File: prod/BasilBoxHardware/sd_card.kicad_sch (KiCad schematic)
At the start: 1 part

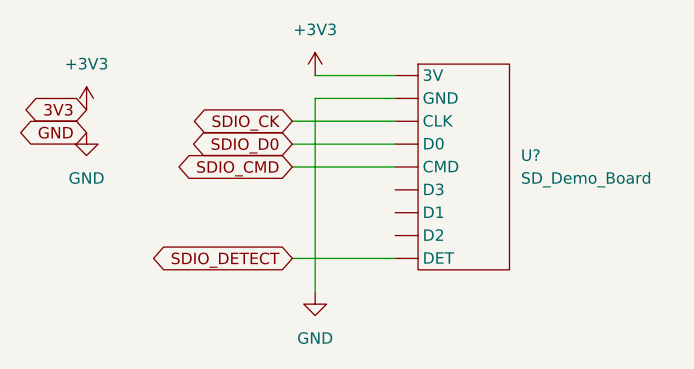
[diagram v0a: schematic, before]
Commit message: Finish schematic
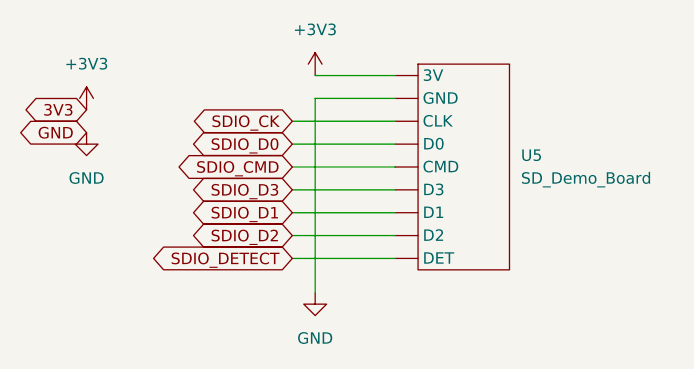
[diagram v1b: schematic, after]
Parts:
- gave numbers to parts that had none: 1
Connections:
- new net SDIO_D1: U5. (GND)
- new net SDIO_D2: U5. (GND)
- new net SDIO_D3: U5. (GND)
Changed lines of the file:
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@@
+    (stroke (width 0) (type default) (color 0 0 0 0))
+  )
+  (wire (pts (xy 139.7 81.28) (xy 151.13 81.28))
+    (stroke (width 0) (type default) (color 0 0 0 0))
+  )
+  (wire (pts (xy 139.7 78.74) (xy 151.13 78.74))
     (stroke (width 0) (type default) (color 0 0 0 0))
   )
@@
   )
   (wire (pts (xy 139.7 86.36) (xy 151.13 86.36))
+    (stroke (width 0) (type default) (color 0 0 0 0))
+  )
+  (wire (pts (xy 139.7 83.82) (xy 151.13 83.82))
     (stroke (width 0) (type default) (color 0 0 0 0))
   )
@@
     (effects (font (size 1.27 1.27)) (justify right))
     (property "Intersheet References" "${INTERSHEET_REFS}" (id 0) (at 129.425 73.5806 0)
+      (effects (font (size 1.27 1.27)) (justify right) hide)
+    )
+  )
+  (global_label "SDIO_D2" (shape bidirectional) (at 139.7 83.82 180) (fields_autoplaced)
+    (effects (font (size 1.27 1.27)) (justify right))
+    (property "Intersheet References" "${INTERSHEET_REFS}" (id 0) (at 129.425 83.7406 0)
+      (effects (font (size 1.27 1.27)) (justify right) hide)
+    )
+  )
+  (global_label "SDIO_D1" (shape bidirectional) (at 139.7 81.28 180) (fields_autoplaced)
+    (effects (font (size 1.27 1.27)) (justify right))
+    (property "Intersheet References" "${INTERSHEET_REFS}" (id 0) (at 129.425 81.2006 0)
+      (effects (font (size 1.27 1.27)) (justify right) hide)
+    )
+  )
+  (global_label "SDIO_D3" (shape bidirectional) (at 139.7 78.74 180) (fields_autoplaced)
+    (effects (font (size 1.27 1.27)) (justify right))
+    (property "Intersheet References" "${INTERSHEET_REFS}" (id 0) (at 129.425 78.6606 0)
       (effects (font (size 1.27 1.27)) (justify right) hide)
     )
@@
   (symbol (lib_id "Connector:SD_Demo_Board") (at 153.67 64.77 0) (unit 1)
     (in_bom yes) (on_board yes) (fields_autoplaced)
-    (property "Reference" "U?" (id 0) (at 165.1 74.9299 0)
+    (property "Reference" "U5" (id 0) (at 165.1 74.9299 0)
       (effects (font (size 1.27 1.27)) (justify left))
     )
